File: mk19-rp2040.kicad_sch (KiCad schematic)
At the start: 134 parts, among them J1 USB_C_Receptacle_USB2.0, J10 Conn_01x02, J11 Conn_01x03_Socket, J12 USB_C_Receptacle_USB2.0, J13 USB_C_Receptacle_USB2.0, J3 Conn_01x02_Socket, J5 Conn_01x02, J7 Conn_01x02_Socket, J8 Conn_01x02_Socket, J9 Conn_01x02_Socket, T1 Conn_01x01_Socket, T10 Conn_01x01_Socket, T11 Conn_01x01_Socket, T12 Conn_01x01_Socket, T13 Conn_01x01_Socket, T14 Conn_01x01_Socket, T15 Conn_01x01_Socket, T2 Conn_01x01_Socket, T3 Conn_01x01_Socket, T5 Conn_01x01_Socket, T6 Conn_01x01_Socket, T7 Conn_01x01_Socket, T8 Conn_01x01_Socket, T9 Conn_01x01_Socket, U1 RP2040, U10 1N4148W_C81598, U11 1N4148W_C81598, U12 1N4148W_C81598, U13 1N4148W_C81598, U14 1N4148W_C81598, U15 1N4148W_C81598, U2 USBLC6-2P6, U3 XC6210B332MR-G, U4 USBLC6-2P6, U5 W25Q128JVS, U6 8_01A0_008200, U7 8_01A0_008200, U8 USBLC6-2P6, U9 1N4148W_C81598, Y1 Crystal_GND24

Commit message: some bad footprints, other fixes
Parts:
- 5WAY1, FAL1, FAL2, PWM1: footprint Connector_JST:JST_XH_B3B-XH-AM_1x08_P2.50mm_Horizontal -> Connector_JST:JST_XH_S8B-XH-A_1x08_P2.50mm_Horizontal
- COL1, COL2, ROW1, ROW2: footprint Connector_JST:JST_EH_S8B-EH_1x08_P2.50mm_Horizontal -> Connector_JST:JST_XH_S8B-XH-A_1x08_P2.50mm_Horizontal
- J1, J12, J13: footprint drawings:GT-USB-7014C -> ct-kicad:USB-C-SMD_12P-P0.50-H-F_TYPE-C-31-M-14
- J3, J7, J8, J9, PWR-EXT-IN1: footprint Connector_JST:JST_XH_B3B-XH-AM_1x02_P2.50mm_Vertical -> Connector_JST:JST_XH_B2B-XH-AM_1x02_P2.50mm_Vertical
- VANILED1: footprint Connector_JST:JST_XH_B3B-XH-AM_1x08_P2.50mm_Vertical -> Connector_JST:JST_XH_B8B-XH-AM_1x08_P2.50mm_Vertical
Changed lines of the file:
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@@
 			)
 		)
-		(property "Footprint" "Connector_JST:JST_XH_B3B-XH-AM_1x08_P2.50mm_Horizontal"
+		(property "Footprint" "Connector_JST:JST_XH_S8B-XH-A_1x08_P2.50mm_Horizontal"
 			(at 158.75 271.78 0)
 			(effects
@@
 			)
 		)
-		(property "Footprint" "Connector_JST:JST_XH_B3B-XH-AM_1x08_P2.50mm_Horizontal"
+		(property "Footprint" "Connector_JST:JST_XH_S8B-XH-A_1x08_P2.50mm_Horizontal"
 			(at 100.33 269.24 0)
 			(effects
@@
 			)
 		)
-		(property "Footprint" "drawings:GT-USB-7014C"
+		(property "Footprint" "ct-kicad:USB-C-SMD_12P-P0.50-H-F_TYPE-C-31-M-14"
 			(at 373.38 367.03 0)
 			(effects
@@
 			)
 		)
-		(property "Footprint" "Connector_JST:JST_XH_B3B-XH-AM_1x02_P2.50mm_Vertical"
+		(property "Footprint" "Connector_JST:JST_XH_B2B-XH-AM_1x02_P2.50mm_Vertical"
 			(at 229.87 429.26 0)
 			(effects
@@
 			)
 		)
-		(property "Footprint" "Connector_JST:JST_XH_B3B-XH-AM_1x02_P2.50mm_Vertical"
+		(property "Footprint" "Connector_JST:JST_XH_B2B-XH-AM_1x02_P2.50mm_Vertical"
 			(at 134.62 411.48 0)
 			(effects
@@
 			)
 		)
-		(property "Footprint" "Connector_JST:JST_XH_B3B-XH-AM_1x08_P2.50mm_Horizontal"
+		(property "Footprint" "Connector_JST:JST_XH_S8B-XH-A_1x08_P2.50mm_Horizontal"
 			(at 46.99 269.24 0)
 			(effects
@@
 			)
 		)
-		(property "Footprint" "drawings:GT-USB-7014C"
+		(property "Footprint" "ct-kicad:USB-C-SMD_12P-P0.50-H-F_TYPE-C-31-M-14"
 			(at 374.65 237.49 0)
 			(effects
@@
 			)
 		)
-		(property "Footprint" "Connector_JST:JST_EH_S8B-EH_1x08_P2.50mm_Horizontal"
+		(property "Footprint" "Connector_JST:JST_XH_S8B-XH-A_1x08_P2.50mm_Horizontal"
 			(at 44.45 148.59 0)
 			(effects
@@
 			)
 		)
-		(property "Footprint" "Connector_JST:JST_EH_S8B-EH_1x08_P2.50mm_Horizontal"
+		(property "Footprint" "Connector_JST:JST_XH_S8B-XH-A_1x08_P2.50mm_Horizontal"
 			(at 71.12 148.59 0)
 			(effects
@@
 			)
 		)
-		(property "Footprint" "Connector_JST:JST_XH_B3B-XH-AM_1x02_P2.50mm_Vertical"
+		(property "Footprint" "Connector_JST:JST_XH_B2B-XH-AM_1x02_P2.50mm_Vertical"
 			(at 209.55 403.86 0)
 			(effects
@@
 			)
 		)
-		(property "Footprint" "Connector_JST:JST_EH_S8B-EH_1x08_P2.50mm_Horizontal"
+		(property "Footprint" "Connector_JST:JST_XH_S8B-XH-A_1x08_P2.50mm_Horizontal"
 			(at 71.12 123.19 0)
 			(effects
@@
 			)
 		)
-		(property "Footprint" "Connector_JST:JST_XH_B3B-XH-AM_1x08_P2.50mm_Vertical"
+		(property "Footprint" "Connector_JST:JST_XH_B8B-XH-AM_1x08_P2.50mm_Vertical"
 			(at 166.37 370.84 0)
 			(effects
@@
 			)
 		)
-		(property "Footprint" "drawings:GT-USB-7014C"
+		(property "Footprint" "ct-kicad:USB-C-SMD_12P-P0.50-H-F_TYPE-C-31-M-14"
 			(at 373.38 302.26 0)
 			(effects
@@
 			)
 		)
-		(property "Footprint" "Connector_JST:JST_XH_B3B-XH-AM_1x02_P2.50mm_Vertical"
+		(property "Footprint" "Connector_JST:JST_XH_B2B-XH-AM_1x02_P2.50mm_Vertical"
 			(at 118.11 331.47 0)
 			(effects
@@
 			)
 		)
-		(property "Footprint" "Connector_JST:JST_EH_S8B-EH_1x08_P2.50mm_Horizontal"
+		(property "Footprint" "Connector_JST:JST_XH_S8B-XH-A_1x08_P2.50mm_Horizontal"
 			(at 44.45 123.19 0)
 			(effects
@@
 			)
 		)
-		(property "Footprint" "Connector_JST:JST_XH_B3B-XH-AM_1x02_P2.50mm_Vertical"
+		(property "Footprint" "Connector_JST:JST_XH_B2B-XH-AM_1x02_P2.50mm_Vertical"
 			(at 248.92 403.86 0)
 			(effects
@@
 			)
 		)
-		(property "Footprint" "Connector_JST:JST_XH_B3B-XH-AM_1x08_P2.50mm_Horizontal"
+		(property "Footprint" "Connector_JST:JST_XH_S8B-XH-A_1x08_P2.50mm_Horizontal"
 			(at 203.2 271.78 0)
 			(effects

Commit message: progress update
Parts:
- J1, J12, J13: symbol Connector:USB_C_Receptacle_USB2.0 -> ct-kicad:TYPE-C-31-M-14
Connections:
- net GND: now also J1.A1B12 (GND), J1.B1A12 (GND), J12.A1B12 (GND), J12.B1A12 (GND), J13.A1B12 (GND), J13.B1A12 (GND); no longer J1.A1 (GND), J1.A12 (GND), J1.B1 (GND), J1.B12 (GND), J12.A1 (GND), J12.A12 (GND), J12.B1 (GND), J12.B12 (GND), J13.A1 (GND), J13.A12 (GND), J13.B1 (GND), J13.B12 (GND)
- net LED_SCREEN_DI: now also J13.A7 (DN1), J13.B7 (DN2); no longer J13.A6 (D+), J13.B6 (D+)
- net LED_SCREEN_DO: now also J13.A6 (DP1), J13.B6 (DP2); no longer J13.A7 (D-), J13.B7 (D-)
- net Serial_VBUS: now also J12.A4B9 (VBUS), J12.B4A9 (VBUS), J13.A4B9 (VBUS), J13.B4A9 (VBUS); no longer J12.A4 (VBUS), J12.A9 (VBUS), J12.B4 (VBUS), J12.B9 (VBUS), J13.A4 (VBUS), J13.A9 (VBUS), J13.B4 (VBUS), J13.B9 (VBUS)
- net Split_Comms_RX: now also J12.A6 (DP1), J12.B6 (DP2); no longer J12.A7 (D-), J12.B7 (D-)
- net Split_Comms_TX: now also J12.A7 (DN1), J12.B7 (DN2); no longer J12.A6 (D+), J12.B6 (D+)
- net USB-MAIN_+: now also J1.A7 (DN1), J1.B7 (DN2); no longer J1.A6 (D+), J1.B6 (D+)
- net USB-MAIN_-: now also J1.A6 (DP1), J1.B6 (DP2); no longer J1.A7 (D-), J1.B7 (D-)
- net VBUS: now also J1.A4B9 (VBUS), J1.B4A9 (VBUS); no longer J1.A4 (VBUS), J1.A9 (VBUS), J1.B4 (VBUS), J1.B9 (VBUS)
- net at FB3.2: now also J13.S (SHIELD); no longer J13.S1 (SHIELD)
- net at FB2.2: now also J12.S (SHIELD); no longer J12.S1 (SHIELD)
- net at FB1.2: now also J1.S (SHIELD); no longer J1.S1 (SHIELD)
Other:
- moved on the sheet: FB1, FB2, FB3

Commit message: fixes
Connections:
- net +5V: now also J13.A4B9 (VBUS), J13.B4A9 (VBUS)
- net Serial_VBUS: no longer J13.A4B9 (VBUS), J13.B4A9 (VBUS)
- net VBUS_DET: now also U1.40 (GPIO28_ADC2); no longer U1.41 (GPIO29_ADC3)
- net at T6.1 (Pin_1): now also U1.41 (GPIO29_ADC3); no longer U1.40 (GPIO28_ADC2)
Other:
- moved on the sheet: R10, R11, T6

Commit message: getting close to having the rp2040 traced
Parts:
- removed 5WAY1: Conn_01x08_Socket, Connector_JST:JST_XH_S8B-XH-A_1x08_P2.50mm_Horizontal, symbol Connector:Conn_01x08_Socket
- removed T8: Conn_01x01_Socket, Connector_Pin:Pin_D1.0mm_L10.0mm, symbol Connector:Conn_01x01_Socket
- added J2: Conn_01x03_Socket, Connector_JST:JST_XH_S3B-XH-A_1x03_P2.50mm_Horizontal, symbol Connector:Conn_01x03_Socket
- added J4: Conn_01x06_Socket, Connector_JST:JST_XH_S6B-XH-A_1x06_P2.50mm_Horizontal, symbol Connector:Conn_01x06_Socket
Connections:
- net GND: now also J2.3 (Pin_3)
- net Serial-RX: no longer U1.2 (GPIO0)
- net VANILED_SIG3: no longer U1.37 (GPIO25)
- net VANILED_SIG4: now also U1.37 (GPIO25)
- net rkjxt-a: now also J2.2 (Pin_2)
- net rkjxt-b: now also J2.1 (Pin_1)
- net row5: now also J4.5 (Pin_5)
- net at U10.2 (A): now also J4.3 (Pin_3)
- net at U11.2 (A): now also J4.1 (Pin_1)
- net at U13.2 (A): now also J4.2 (Pin_2)
- net at U9.2 (A): now also J4.6 (Pin_6)
- net at U12.2 (A): now also J4.4 (Pin_4)
- new net Serial-TX: U1.2 (GPIO0)
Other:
- note added: "5-way switch (dpad)"
- note added: "RKJXT extender"
- moved on the sheet: R13, R14, U10, U11, U12, U13, U9

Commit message: more progress
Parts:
- AUDIO1, J11, PWR-OUT1: footprint Connector_JST:JST_XH_B3B-XH-AM_1x03_P2.50mm_Vertical -> Connector_JST:JST_XH_B3B-XH-A_1x03_P2.50mm_Vertical
- COL1, COL2, ROW1, ROW2: footprint Connector_JST:JST_XH_S8B-XH-A_1x08_P2.50mm_Horizontal -> Connector_JST:JST_XH_B8B-XH-A_1x08_P2.50mm_Vertical
- J3, J7, J8, J9, PWR-EXT-IN1: footprint Connector_JST:JST_XH_B2B-XH-AM_1x02_P2.50mm_Vertical -> Connector_JST:JST_XH_B2B-XH-A_1x02_P2.50mm_Vertical
- PWR-OUT3: footprint Connector_JST:JST_XH_B3B-XH-AM_1x03_P2.50mm_Vertical -> Connector_PinHeader_2.54mm:PinHeader_1x03_P2.54mm_Vertical
- VANILED1: footprint Connector_JST:JST_XH_B8B-XH-AM_1x08_P2.50mm_Vertical -> Connector_JST:JST_XH_B8B-XH-A_1x08_P2.50mm_Vertical
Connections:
- net VCC is gone; now on net +5V: C19.1, LED-LVL1.6 (VCCB)
- net +3V3: now also R20.1; no longer C10.1
- net +5V: no longer R20.1
- net AUDIO: now also U1.2 (GPIO0); no longer U1.38 (GPIO26_ADC0)
- net GND: no longer C10.2
- net Serial-RX: now also U1.41 (GPIO29_ADC3); no longer U1.3 (GPIO1)
- net Serial-TX: now also U1.40 (GPIO28_ADC2); no longer U1.2 (GPIO0)
- net VANILED_SIG1: now also VANILED1.6 (Pin_6); no longer VANILED1.3 (Pin_3)
- net VANILED_SIG2: now also VANILED1.5 (Pin_5); no longer VANILED1.4 (Pin_4)
- net VANILED_SIG3: now also VANILED1.4 (Pin_4); no longer VANILED1.5 (Pin_5)
- net VANILED_SIG4: now also VANILED1.3 (Pin_3); no longer VANILED1.6 (Pin_6)
- net VBUS_DET: now also U1.3 (GPIO1); no longer U1.40 (GPIO28_ADC2)
- net at T5.1 (Pin_1): now also U1.38 (GPIO26_ADC0); no longer U1.39 (GPIO27_ADC1)
- net at T6.1 (Pin_1): now also U1.39 (GPIO27_ADC1); no longer U1.41 (GPIO29_ADC3)
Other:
- moved on the sheet: C10, R10, R11, T5, T6

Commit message: even more progress, starting to come together.
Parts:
- J10, J5: footprint drawings:PinHeader_1x02_P1.27mm_Vertical -> Connector_PinSocket_2.54mm:PinSocket_1x02_P2.54mm_Vertical
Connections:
- net fal2-r1: now also U1.5 (GPIO3); no longer U1.9 (GPIO7)
- net fal2-r2: now also U1.6 (GPIO4); no longer U1.11 (GPIO8)
- net rkjxt-a: now also U1.11 (GPIO8); no longer U1.5 (GPIO3)
- net rkjxt-b: now also U1.9 (GPIO7); no longer U1.6 (GPIO4)
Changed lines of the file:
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@@
 		)
 	)
-	(global_label "fal1-r1"
-		(shape output)
-		(at 504.19 77.47 0)
+	(global_label "row5"
+		(shape input)
+		(at 72.39 78.74 180)
 		(fields_autoplaced yes)
 		(effects
@@
 				(size 1.27 1.27)
 			)
-			(justify left)
+			(justify right)
 		)
 		(property "Intersheetrefs" "${INTERSHEET_REFS}"
-			(at 514.4927 77.47 0)
+			(at 64.9296 78.74 0)
 			(effects
 				(font
 					(size 1.27 1.27)
 				)
-				(justify left)
+				(justify right)
 				(hide yes)
 			)
 		)
 	)
-	(global_label "row5"
-		(shape input)
-		(at 72.39 78.74 180)
+	(global_label "col7"
+		(shape output)
+		(at 273.05 62.23 0)
 		(fields_autoplaced yes)
 		(effects
@@
 				(size 1.27 1.27)
 			)
-			(justify right)
+			(justify left)
 		)
 		(property "Intersheetrefs" "${INTERSHEET_REFS}"
-			(at 64.9296 78.74 0)
+			(at 280.1475 62.23 0)
 			(effects
 				(font
 					(size 1.27 1.27)
 				)
-				(justify right)
+				(justify left)
 				(hide yes)
 			)
 		)
 	)
-	(global_label "col7"
+	(global_label "fal2-r1"
 		(shape output)
-		(at 273.05 62.23 0)
+		(at 504.19 72.39 0)
 		(fields_autoplaced yes)
 		(effects
@@
 		)
 		(property "Intersheetrefs" "${INTERSHEET_REFS}"
-			(at 280.1475 62.23 0)
+			(at 514.4927 72.39 0)
 			(effects
 				(font
@@
 		)
 	)
-	(global_label "fal2-r2"
-		(shape output)
-		(at 504.19 85.09 0)
-		(fields_autoplaced yes)
-		(effects
-			(font
-				(size 1.27 1.27)
-			)
-			(justify left)
-		)
-		(property "Intersheetrefs" "${INTERSHEET_REFS}"
-			(at 514.4927 85.09 0)
-			(effects
-				(font
-					(size 1.27 1.27)
-				)
-				(justify left)
-				(hide yes)
-			)
-		)
-	)
 	(global_label "fal1-r2"
 		(shape input)
@@
 		)
 	)
-	(global_label "LED_MACRO_DI"
-		(shape input)
-		(at 247.65 69.85 180)
+	(global_label "fal1-r1"
+		(shape output)
+		(at 504.19 77.47 0)
 		(fields_autoplaced yes)
 		(effects
@@
 				(size 1.27 1.27)
 			)
-			(justify right)
+			(justify left)
 		)
 		(property "Intersheetrefs" "${INTERSHEET_REFS}"
-			(at 230.9972 69.85 0)
+			(at 514.4927 77.47 0)
 			(effects
 				(font
 					(size 1.27 1.27)
 				)
-				(justify right)
+				(justify left)
 				(hide yes)
 			)
 		)
 	)
-	(global_label "row1"
+	(global_label "LED_MACRO_DI"
 		(shape input)
-		(at 53.34 115.57 0)
+		(at 247.65 69.85 180)
 		(fields_autoplaced yes)
 		(effects
@@
 				(size 1.27 1.27)
 			)
-			(justify left)
+			(justify right)
 		)
 		(property "Intersheetrefs" "${INTERSHEET_REFS}"
-			(at 60.8004 115.57 0)
+			(at 230.9972 69.85 0)
 			(effects
 				(font
 					(size 1.27 1.27)
 				)
-				(justify left)
+				(justify right)
 				(hide yes)
 			)
 		)
 	)
-	(global_label "rkjxt-a"
-		(shape output)
-		(at 504.19 72.39 0)
+	(global_label "row1"
+		(shape input)
+		(at 53.34 115.57 0)
 		(fields_autoplaced yes)
 		(effects
@@
 		)
 		(property "Intersheetrefs" "${INTERSHEET_REFS}"
-			(at 514.0695 72.39 0)
+			(at 60.8004 115.57 0)
 			(effects
 				(font
@@
 		)
 	)
+	(global_label "fal2-r2"
+		(shape output)
+		(at 504.19 74.93 0)
+		(fields_autoplaced yes)
+		(effects
+			(font
+				(size 1.27 1.27)
+			)
+			(justify left)
+		)
+		(property "Intersheetrefs" "${INTERSHEET_REFS}"
+			(at 514.4927 74.93 0)
+			(effects
+				(font
+					(size 1.27 1.27)
+				)
+				(justify left)
+				(hide yes)
+			)
+		)
+	)
 	(global_label "row8"
 		(shape input)
@@
 		)
 	)
-	(global_label "fal1-r2"
-		(shape output)
-		(at 504.19 80.01 0)
-		(fields_autoplaced yes)
-		(effects
-			(font
-				(size 1.27 1.27)
-			)
-			(justify left)
-		)
-		(property "Intersheetrefs" "${INTERSHEET_REFS}"
-			(at 514.4927 80.01 0)
-			(effects
-				(font
-					(size 1.27 1.27)
-				)
-				(justify left)
-				(hide yes)
-			)
-		)
-	)
 	(global_label "row0"
 		(shape output)
@@
 		)
 	)
-	(global_label "rkjxt-b"
-		(shape output)
-		(at 504.19 74.93 0)
-		(fields_autoplaced yes)
-		(effects
-			(font
-				(size 1.27 1.27)
-			)
-			(justify left)
-		)
-		(property "Intersheetrefs" "${INTERSHEET_REFS}"
-			(at 514.0695 74.93 0)
-			(effects
-				(font
-					(size 1.27 1.27)
-				)
-				(justify left)
-				(hide yes)
-			)
-		)
-	)
 	(global_label "col1"
 		(shape output)
@@
 		)
 	)
-	(global_label "fal2-r1"
-		(shape output)
-		(at 504.19 82.55 0)
-		(fields_autoplaced yes)
-		(effects
-			(font
-				(size 1.27 1.27)
-			)
-			(justify left)
-		)
-		(property "Intersheetrefs" "${INTERSHEET_REFS}"
-			(at 514.4927 82.55 0)
-			(effects
-				(font
-					(size 1.27 1.27)
-				)
-				(justify left)
-				(hide yes)
-			)
-		)
-	)
 	(global_label "SPI1_CLK"
 		(shape input)
@@
 		)
 	)
+	(global_label "rkjxt-b"
+		(shape output)
+		(at 504.19 82.55 0)
+		(fields_autoplaced yes)
+		(effects
+			(font
+				(size 1.27 1.27)
+			)
+			(justify left)
+		)
+		(property "Intersheetrefs" "${INTERSHEET_REFS}"
+			(at 514.0695 82.55 0)
+			(effects
+				(font
+					(size 1.27 1.27)
+				)
+				(justify left)
+				(hide yes)
+			)
+		)
+	)
 	(global_label "col4"
 		(shape output)
@@
 		)
 	)
+	(global_label "fal1-r2"
+		(shape output)
+		(at 504.19 80.01 0)
+		(fields_autoplaced yes)
+		(effects
+			(font
+				(size 1.27 1.27)
+			)
+			(justify left)
+		)
+		(property "Intersheetrefs" "${INTERSHEET_REFS}"
+			(at 514.4927 80.01 0)
+			(effects
+				(font
+					(size 1.27 1.27)
+				)
+				(justify left)
+				(hide yes)
+			)
+		)
+	)
 	(global_label "row5"
 		(shape input)
@@
 		)
 	)
+	(global_label "rkjxt-a"
+		(shape output)
+		(at 504.19 85.09 0)
+		(fields_autoplaced yes)
+		(effects
+			(font
+				(size 1.27 1.27)
+			)
+			(justify left)
+		)
+		(property "Intersheetrefs" "${INTERSHEET_REFS}"
+			(at 514.0695 85.09 0)
+			(effects
+				(font
+					(size 1.27 1.27)
+				)
+				(justify left)
+				(hide yes)
+			)
+		)
+	)
 	(global_label "row11"
 		(shape output)
@@
 			)
 		)
-		(property "Footprint" "drawings:PinHeader_1x02_P1.27mm_Vertical"
+		(property "Footprint" "Connector_PinSocket_2.54mm:PinSocket_1x02_P2.54mm_Vertical"
 			(at 354.33 189.23 0)
 			(effects
@@
 			)
 		)
-		(property "Footprint" "drawings:PinHeader_1x02_P1.27mm_Vertical"
+		(property "Footprint" "Connector_PinSocket_2.54mm:PinSocket_1x02_P2.54mm_Vertical"
 			(at 410.21 123.19 0)
 			(effects

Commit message: almost done
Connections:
- net Split_Comms_RX is gone; now on net Serial-RX: J12.A6 (DP1), J12.B6 (DP2), U8.1 (I/O1), U8.6 (I/O1)
- net Split_Comms_TX is gone; now on net Serial-TX: J12.A7 (DN1), J12.B7 (DN2), U8.3 (I/O2), U8.4 (I/O2)
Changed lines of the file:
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@@
 	)
 	(global_label "Serial-RX"
-		(shape input)
+		(shape bidirectional)
 		(at 504.19 140.97 0)
 		(fields_autoplaced yes)
@@
 		)
 		(property "Intersheetrefs" "${INTERSHEET_REFS}"
-			(at 516.7304 140.97 0)
+			(at 517.8417 140.97 0)
 			(effects
 				(font
@@
 		)
 	)
-	(global_label "Split_Comms_RX"
+	(global_label "Serial-RX"
 		(shape bidirectional)
 		(at 439.42 302.26 0)
@@
 		)
 		(property "Intersheetrefs" "${INTERSHEET_REFS}"
-			(at 459.1191 302.26 0)
+			(at 453.0717 302.26 0)
 			(effects
 				(font
@@
 	)
 	(global_label "Serial-TX"
-		(shape output)
+		(shape bidirectional)
 		(at 504.19 138.43 0)
 		(fields_autoplaced yes)
@@
 		)
 		(property "Intersheetrefs" "${INTERSHEET_REFS}"
-			(at 516.428 138.43 0)
+			(at 517.5393 138.43 0)
 			(effects
 				(font
@@
 		)
 	)
-	(global_label "Split_Comms_TX"
+	(global_label "Serial-TX"
 		(shape bidirectional)
 		(at 439.42 327.66 0)
@@
 		)
 		(property "Intersheetrefs" "${INTERSHEET_REFS}"
-			(at 458.8167 327.66 0)
-			(effects
-				(font
+			(at 452.7693 327.66 0)
+			(effects
+				(font

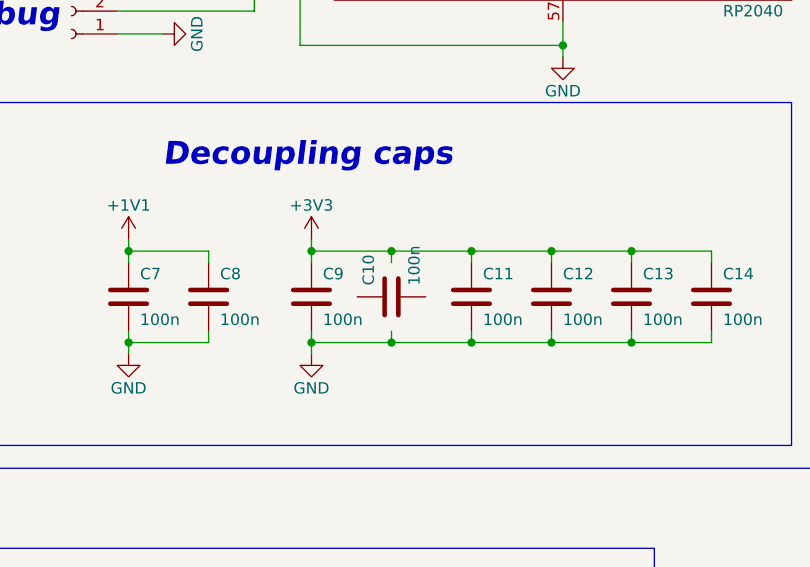
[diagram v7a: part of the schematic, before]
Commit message: drc passing, everything hooked up
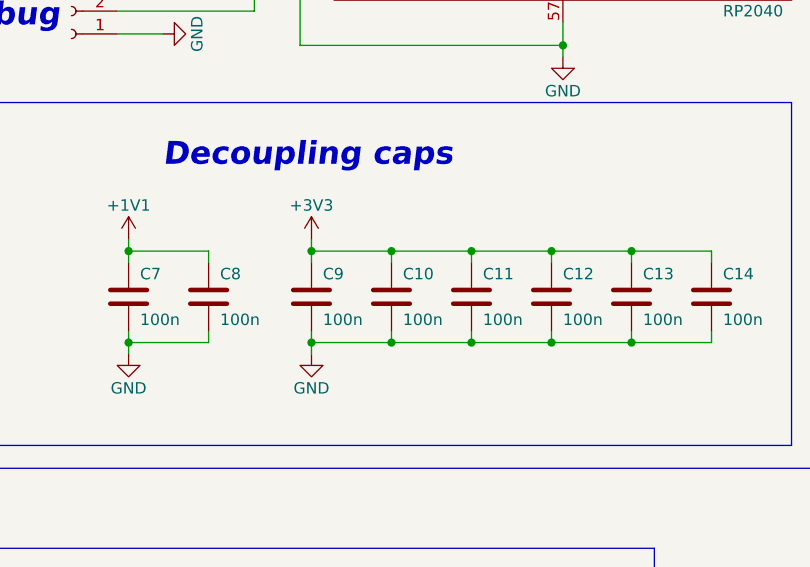
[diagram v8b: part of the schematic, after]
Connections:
- net +3V3: now also C10.1
- net GND: now also C10.2
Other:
- moved on the sheet: C10
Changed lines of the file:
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@@
 	(symbol
 		(lib_id "Device:C")
-		(at 440.69 179.07 90)
+		(at 440.69 179.07 0)
 		(unit 1)
 		(exclude_from_sim no)
@@
 		(dnp no)
 		(property "Reference" "C10"
-			(at 438.15 177.8 0)
+			(at 441.96 176.53 0)
 			(effects
 				(font
@@
 		)
 		(property "Value" "100n"
-			(at 443.23 177.8 0)
+			(at 441.96 181.61 0)
 			(effects
 				(font
@@
 		)
 		(property "Footprint" "Capacitor_SMD:C_0402_1005Metric"
-			(at 444.5 178.1048 0)
+			(at 441.6552 182.88 0)
 			(effects
 				(font
